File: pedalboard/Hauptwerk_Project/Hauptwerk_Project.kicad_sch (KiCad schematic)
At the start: 44 parts, among them J1 Power 5V, J2 1-6, J3 7-12, J4 13-18, J5 19-24, J6 25-30, J7 31-32, J8 Interface to Arduino, U1 74HC165, U2 74HC165, U3 74HC165, U4 74HC165

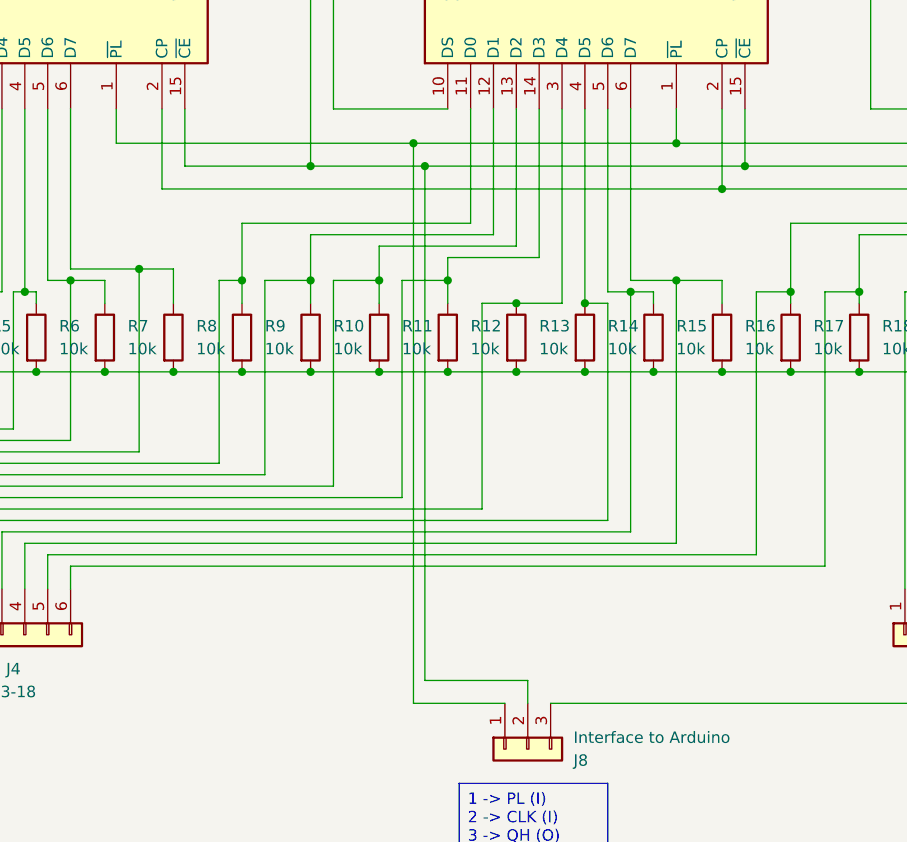
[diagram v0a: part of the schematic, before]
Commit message: Creazione PCB
Prima versione creata e qualche sistemazione nello schema elettrico
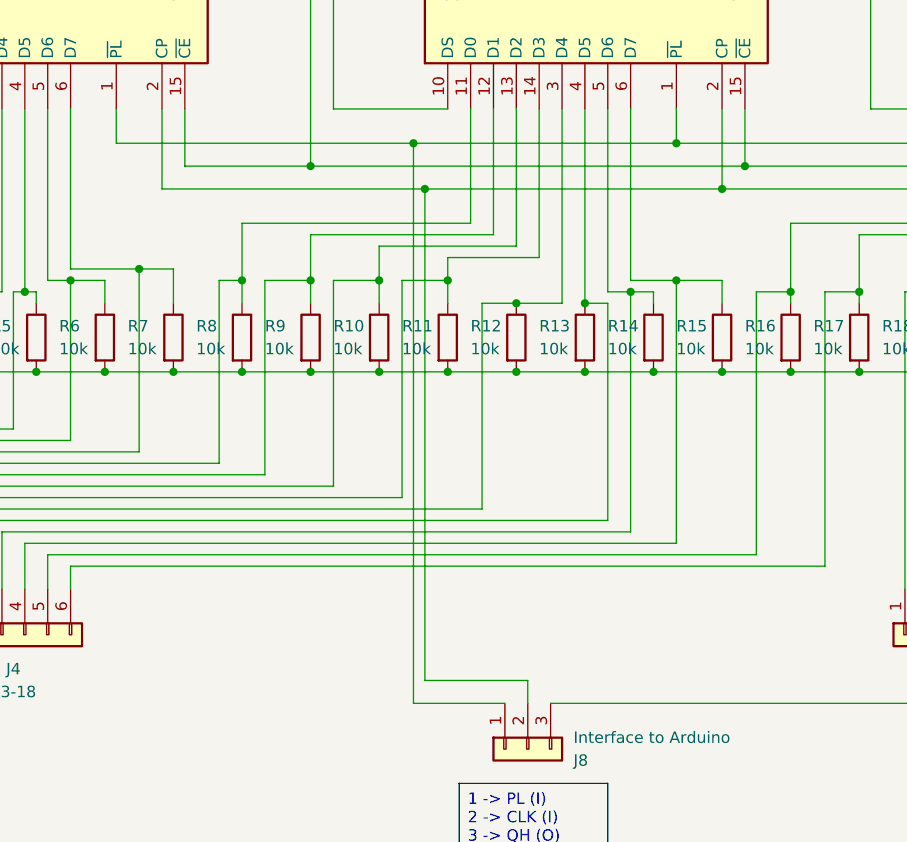
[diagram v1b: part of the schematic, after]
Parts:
- J1, J7: footprint (none) -> TerminalBlock_Phoenix:TerminalBlock_Phoenix_MKDS-1,5-2-5.08_1x02_P5.08mm_Horizontal
- J2, J3, J4, J5, J6: footprint (none) -> TerminalBlock_Phoenix:TerminalBlock_Phoenix_MKDS-1,5-6-5.08_1x06_P5.08mm_Horizontal
- J8: footprint (none) -> TerminalBlock_Phoenix:TerminalBlock_Phoenix_MKDS-1,5-3-5.08_1x03_P5.08mm_Horizontal
- R1, R10, R11, R12, R13, R14, R15, R16, R17, R18, R19, R2, R20, R21, R22, R23, R24, R25, R26, R27, R28, R29, R3, R30, R31, R32, R4, R5, R6, R7, R8, R9: footprint (none) -> Resistor_THT:R_Axial_DIN0207_L6.3mm_D2.5mm_P7.62mm_Horizontal
- U1, U2, U3, U4: footprint (none) -> Package_DIP:DIP-16_W7.62mm
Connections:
- net GND: no longer J8.2 (Pin_2)
- net at U1.2 (CP), U2.2 (CP), U3.2 (CP)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: now also J8.2 (Pin_2)
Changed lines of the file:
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@@
 	)
 	(junction
+		(at 121.92 62.23)
+		(diameter 0)
+		(color 0 0 0 0)
+	)
+	(junction
 		(at 40.64 82.55)
 		(diameter 0)
@@
 	)
 	(junction
-		(at 121.92 59.69)
-		(diameter 0)
-		(color 0 0 0 0)
-	)
-	(junction
 		(at 63.5 82.55)
 		(diameter 0)
@@
 	(wire
 		(pts
-			(xy 92.71 62.23) (xy 154.94 62.23)
+			(xy 92.71 62.23) (xy 121.92 62.23)
 		)
 		(stroke
@@
 	(wire
 		(pts
-			(xy 121.92 59.69) (xy 157.48 59.69)
+			(xy 109.22 59.69) (xy 157.48 59.69)
 		)
 		(stroke
@@
 	(wire
 		(pts
+			(xy 121.92 62.23) (xy 154.94 62.23)
+		)
+		(stroke
+			(width 0)
+			(type default)
+		)
+	)
+	(wire
+		(pts
 			(xy 116.84 13.97) (xy 116.84 40.64)
 		)
@@
 	(wire
 		(pts
+			(xy 121.92 62.23) (xy 121.92 116.84)
+		)
+		(stroke
+			(width 0)
+			(type default)
+		)
+	)
+	(wire
+		(pts
 			(xy 80.01 72.39) (xy 82.55 72.39)
 		)
@@
 	(wire
 		(pts
-			(xy 121.92 59.69) (xy 121.92 116.84)
-		)
-		(stroke
-			(width 0)
-			(type default)
-		)
-	)
-	(wire
-		(pts
 			(xy 46.99 86.36) (xy 46.99 106.68)
 		)
@@
 	(wire
 		(pts
-			(xy 109.22 59.69) (xy 121.92 59.69)
-		)
-		(stroke
-			(width 0)
-			(type default)
-		)
-	)
-	(wire
-		(pts
 			(xy 116.84 68.58) (xy 116.84 72.39)
 		)
@@
 			)
 		)
-		(property "Footprint" ""
+		(property "Footprint" "TerminalBlock_Phoenix:TerminalBlock_Phoenix_MKDS-1,5-6-5.08_1x06_P5.08mm_Horizontal"
 			(at 74.93 111.76 0)
 			(effects
@@
 			)
 		)
-		(property "Footprint" ""
+		(property "Footprint" "Resistor_THT:R_Axial_DIN0207_L6.3mm_D2.5mm_P7.62mm_Horizontal"
 			(at 244.602 78.74 90)
 			(effects
@@
 			)
 		)
-		(property "Footprint" ""
+		(property "Footprint" "TerminalBlock_Phoenix:TerminalBlock_Phoenix_MKDS-1,5-3-5.08_1x03_P5.08mm_Horizontal"
 			(at 133.35 124.46 0)
 			(effects
@@
 			)
 		)
-		(property "Footprint" ""
+		(property "Footprint" "Resistor_THT:R_Axial_DIN0207_L6.3mm_D2.5mm_P7.62mm_Horizontal"
 			(at 236.982 78.74 90)
 			(effects
@@
 			)
 		)
-		(property "Footprint" ""
+		(property "Footprint" "Resistor_THT:R_Axial_DIN0207_L6.3mm_D2.5mm_P7.62mm_Horizontal"
 			(at 229.362 78.74 90)
 			(effects
@@
 			)
 		)
-		(property "Footprint" ""
+		(property "Footprint" "Resistor_THT:R_Axial_DIN0207_L6.3mm_D2.5mm_P7.62mm_Horizontal"
 			(at 183.642 78.74 90)
 			(effects
@@
 			)
 		)
-		(property "Footprint" ""
+		(property "Footprint" "Resistor_THT:R_Axial_DIN0207_L6.3mm_D2.5mm_P7.62mm_Horizontal"
 			(at 76.962 78.74 90)
 			(effects
@@
 			)
 		)
-		(property "Footprint" ""
+		(property "Footprint" "TerminalBlock_Phoenix:TerminalBlock_Phoenix_MKDS-1,5-6-5.08_1x06_P5.08mm_Horizontal"
 			(at 44.45 111.76 0)
 			(effects
@@
 			)
 		)
-		(property "Footprint" ""
+		(property "Footprint" "TerminalBlock_Phoenix:TerminalBlock_Phoenix_MKDS-1,5-2-5.08_1x02_P5.08mm_Horizontal"
 			(at 205.74 111.76 0)
 			(effects
@@
 			)
 		)
-		(property "Footprint" ""
+		(property "Footprint" "Package_DIP:DIP-16_W7.62mm"
 			(at 139.7 40.64 0)
 			(effects
@@
 			)
 		)
-		(property "Footprint" ""
+		(property "Footprint" "Resistor_THT:R_Axial_DIN0207_L6.3mm_D2.5mm_P7.62mm_Horizontal"
 			(at 198.882 78.74 90)
 			(effects
@@
 			)
 		)
-		(property "Footprint" ""
+		(property "Footprint" "TerminalBlock_Phoenix:TerminalBlock_Phoenix_MKDS-1,5-6-5.08_1x06_P5.08mm_Horizontal"
 			(at 180.34 111.76 0)
 			(effects
@@
 			)
 		)
-		(property "Footprint" ""
+		(property "Footprint" "Resistor_THT:R_Axial_DIN0207_L6.3mm_D2.5mm_P7.62mm_Horizontal"
 			(at 168.402 78.74 90)
 			(effects
@@
 			)
 		)
-		(property "Footprint" ""
+		(property "Footprint" "Resistor_THT:R_Axial_DIN0207_L6.3mm_D2.5mm_P7.62mm_Horizontal"
 			(at 137.922 78.74 90)
 			(effects
@@
 			)
 		)
-		(property "Footprint" ""
+		(property "Footprint" "Resistor_THT:R_Axial_DIN0207_L6.3mm_D2.5mm_P7.62mm_Horizontal"
 			(at 107.442 78.74 90)
 			(effects
@@
 			)
 		)
-		(property "Footprint" ""
+		(property "Footprint" "Resistor_THT:R_Axial_DIN0207_L6.3mm_D2.5mm_P7.62mm_Horizontal"
 			(at 54.102 78.74 90)
 			(effects
@@
 			)
 		)
-		(property "Footprint" ""
+		(property "Footprint" "Resistor_THT:R_Axial_DIN0207_L6.3mm_D2.5mm_P7.62mm_Horizontal"
 			(at 84.582 78.74 90)
 			(effects
@@
 			)
 		)
-		(property "Footprint" ""
+		(property "Footprint" "Resistor_THT:R_Axial_DIN0207_L6.3mm_D2.5mm_P7.62mm_Horizontal"
 			(at 153.162 78.74 90)
 			(effects
@@
 			)
 		)
-		(property "Footprint" ""
+		(property "Footprint" "Resistor_THT:R_Axial_DIN0207_L6.3mm_D2.5mm_P7.62mm_Horizontal"
 			(at 176.022 78.74 90)
 			(effects
@@
 			)
 		)
-		(property "Footprint" ""
+		(property "Footprint" "Resistor_THT:R_Axial_DIN0207_L6.3mm_D2.5mm_P7.62mm_Horizontal"
 			(at 99.822 78.74 90)
 			(effects
@@
 			)
 		)
-		(property "Footprint" ""
+		(property "Footprint" "Resistor_THT:R_Axial_DIN0207_L6.3mm_D2.5mm_P7.62mm_Horizontal"
 			(at 130.302 78.74 90)
 			(effects
@@
 			)
 		)
-		(property "Footprint" ""
+		(property "Footprint" "Resistor_THT:R_Axial_DIN0207_L6.3mm_D2.5mm_P7.62mm_Horizontal"
 			(at 38.862 78.74 90)
 			(effects
@@
 			)
 		)
-		(property "Footprint" ""
+		(property "Footprint" "Resistor_THT:R_Axial_DIN0207_L6.3mm_D2.5mm_P7.62mm_Horizontal"
 			(at 92.202 78.74 90)
 			(effects
@@
 			)
 		)
-		(property "Footprint" ""
+		(property "Footprint" "Resistor_THT:R_Axial_DIN0207_L6.3mm_D2.5mm_P7.62mm_Horizontal"
 			(at 267.462 78.74 90)
 			(effects
@@
 			)
 		)
-		(property "Footprint" ""
+		(property "Footprint" "TerminalBlock_Phoenix:TerminalBlock_Phoenix_MKDS-1,5-6-5.08_1x06_P5.08mm_Horizontal"
 			(at 59.69 111.76 0)
 			(effects
@@
 			)
 		)
-		(property "Footprint" ""
+		(property "Footprint" "Package_DIP:DIP-16_W7.62mm"
 			(at 198.12 40.64 0)
 			(effects
@@
 			)
 		)
-		(property "Footprint" ""
+		(property "Footprint" "Resistor_THT:R_Axial_DIN0207_L6.3mm_D2.5mm_P7.62mm_Horizontal"
 			(at 259.842 78.74 90)
 			(effects
@@
 			)
 		)
-		(property "Footprint" ""
+		(property "Footprint" "Resistor_THT:R_Axial_DIN0207_L6.3mm_D2.5mm_P7.62mm_Horizontal"
 			(at 214.122 78.74 90)
 			(effects
@@
 			)
 		)
-		(property "Footprint" ""
+		(property "Footprint" "Resistor_THT:R_Axial_DIN0207_L6.3mm_D2.5mm_P7.62mm_Horizontal"
 			(at 69.342 78.74 90)
 			(effects
@@
 			)
 		)
-		(property "Footprint" ""
+		(property "Footprint" "Package_DIP:DIP-16_W7.62mm"
 			(at 254 40.64 0)
 			(effects
@@
 			)
 		)
-		(property "Footprint" ""
+		(property "Footprint" "Resistor_THT:R_Axial_DIN0207_L6.3mm_D2.5mm_P7.62mm_Horizontal"
 			(at 61.722 78.74 90)
 			(effects
@@
 			)
 		)
-		(property "Footprint" ""
+		(property "Footprint" "Resistor_THT:R_Axial_DIN0207_L6.3mm_D2.5mm_P7.62mm_Horizontal"
 			(at 145.542 78.74 90)
 			(effects
@@
 			)
 		)
-		(property "Footprint" ""
+		(property "Footprint" "Resistor_THT:R_Axial_DIN0207_L6.3mm_D2.5mm_P7.62mm_Horizontal"
 			(at 160.782 78.74 90)
 			(effects
@@
 			)
 		)
-		(property "Footprint" ""
+		(property "Footprint" "Resistor_THT:R_Axial_DIN0207_L6.3mm_D2.5mm_P7.62mm_Horizontal"
 			(at 115.062 78.74 90)
 			(effects
@@
 			)
 		)
-		(property "Footprint" ""
+		(property "Footprint" "Resistor_THT:R_Axial_DIN0207_L6.3mm_D2.5mm_P7.62mm_Horizontal"
 			(at 206.502 78.74 90)
 			(effects
@@
 			)
 		)
-		(property "Footprint" ""
+		(property "Footprint" "Resistor_THT:R_Axial_DIN0207_L6.3mm_D2.5mm_P7.62mm_Horizontal"
 			(at 221.742 78.74 90)
 			(effects
@@
 			)
 		)
-		(property "Footprint" ""
+		(property "Footprint" "Resistor_THT:R_Axial_DIN0207_L6.3mm_D2.5mm_P7.62mm_Horizontal"
 			(at 122.682 78.74 90)
 			(effects
@@
 			)
 		)
-		(property "Footprint" ""
+		(property "Footprint" "TerminalBlock_Phoenix:TerminalBlock_Phoenix_MKDS-1,5-2-5.08_1x02_P5.08mm_Horizontal"
 			(at 25.4 46.99 0)
 			(effects
@@
 			)
 		)
-		(property "Footprint" ""
+		(property "Footprint" "Resistor_THT:R_Axial_DIN0207_L6.3mm_D2.5mm_P7.62mm_Horizontal"
 			(at 275.082 78.74 90)
 			(effects
@@
 			)
 		)
-		(property "Footprint" ""
+		(property "Footprint" "Resistor_THT:R_Axial_DIN0207_L6.3mm_D2.5mm_P7.62mm_Horizontal"
 			(at 191.262 78.74 90)
 			(effects
@@
 			)
 		)
-		(property "Footprint" ""
+		(property "Footprint" "Package_DIP:DIP-16_W7.62mm"
 			(at 77.47 40.64 0)
 			(effects
@@
 			)
 		)
-		(property "Footprint" ""
+		(property "Footprint" "TerminalBlock_Phoenix:TerminalBlock_Phoenix_MKDS-1,5-6-5.08_1x06_P5.08mm_Horizontal"
 			(at 195.58 111.76 0)
 			(effects
@@
 			)
 		)
-		(property "Footprint" ""
+		(property "Footprint" "Resistor_THT:R_Axial_DIN0207_L6.3mm_D2.5mm_P7.62mm_Horizontal"
 			(at 252.222 78.74 90)
 			(effects
@@
 			)
 		)
-		(property "Footprint" ""
+		(property "Footprint" "Resistor_THT:R_Axial_DIN0207_L6.3mm_D2.5mm_P7.62mm_Horizontal"
 			(at 46.482 78.74 90)
 			(effects
